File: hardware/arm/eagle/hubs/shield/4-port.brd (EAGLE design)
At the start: 31.5 x 58 mm, 11 parts

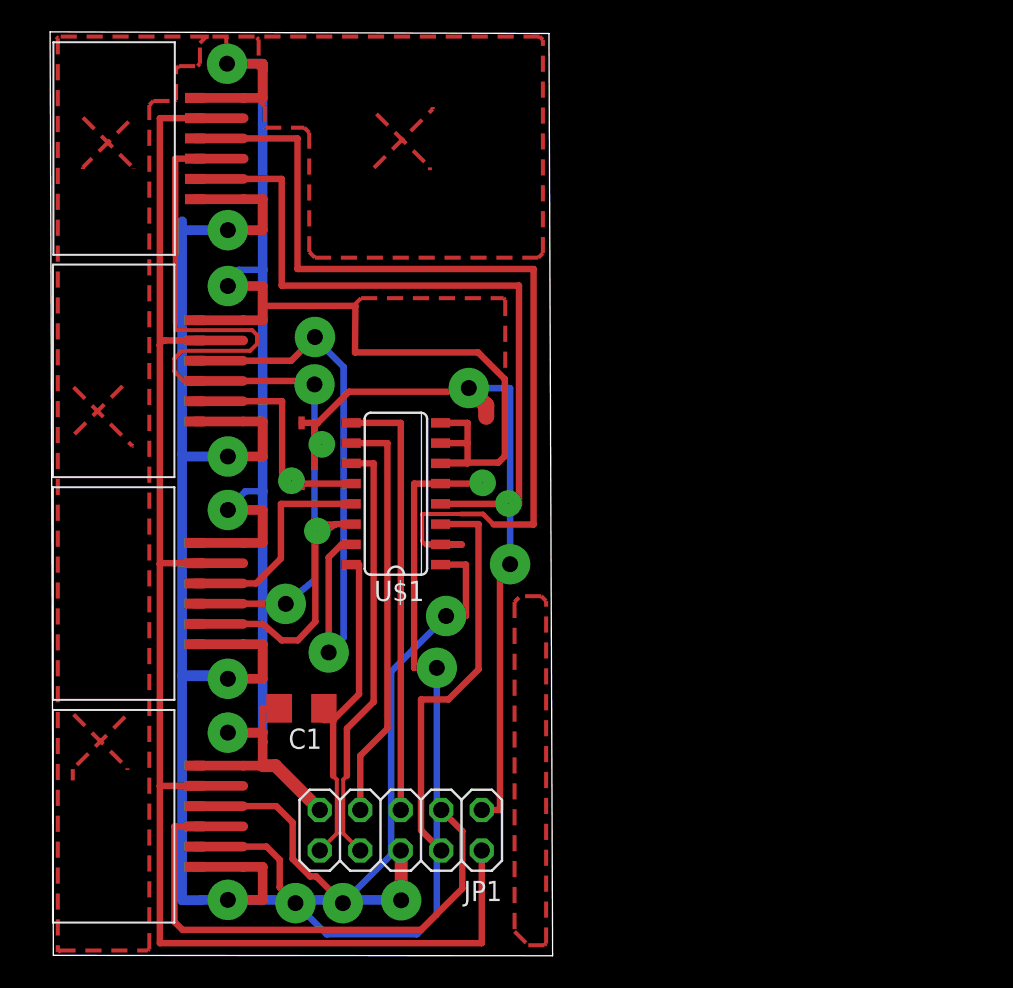
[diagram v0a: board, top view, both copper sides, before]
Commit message: 4 port shield pcb
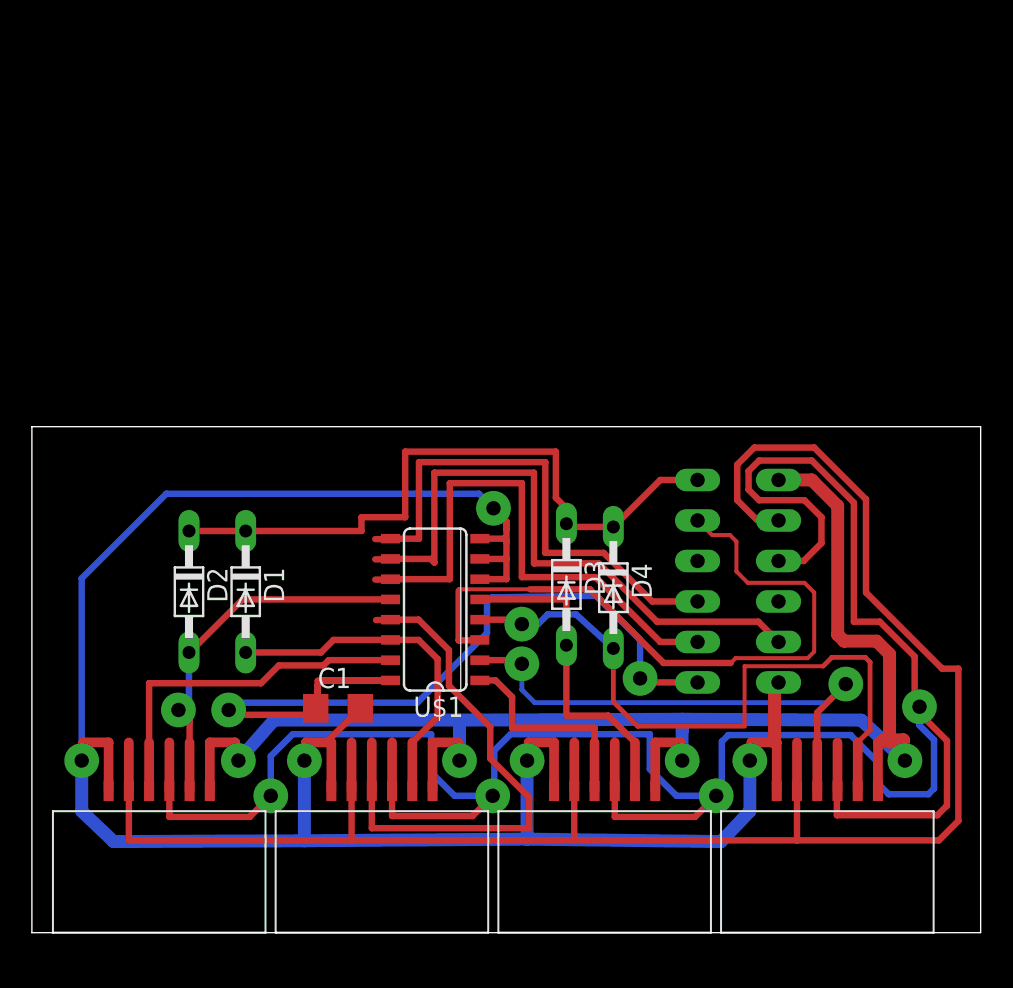
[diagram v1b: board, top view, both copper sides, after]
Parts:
- removed JP1: (no value), pinhead:2X05
- removed U$6, U$8, U$9: DIODE, gumyns:DIL_DIODE_SMD
- added D1, D2, D3, D4: BAS15, diode:DO34-7
- U$3: value DIODE -> HUB_PORT; device gumyns:DIL_DIODE_SMD -> gumyns:HUB_PORT
- moved U$7 63.7 mm to (48.3, 3.81), turned to 0 degrees
- moved U$4 31.9 mm to (6.35, 3.81), turned to 0 degrees
- moved U$5 30.7 mm to (34.3, 3.81), turned to 0 degrees
- moved U$3 27.9 mm to (43.0, 18.2), turned to 90 degrees
- moved U$2 24.3 mm to (20.3, 3.81), turned to 0 degrees
- moved U$1 7.67 mm to (24.0, 20.3)
- moved C1 2.29 mm to (17.9, 14.1), turned to 0 degrees
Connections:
- net 12V: now also U$3.12V; no longer JP1.6
- net 3.3V: now also U$3.3.3V; no longer JP1.10
- net A: now also U$3.A; no longer JP1.8
- net B: now also U$3.B; no longer JP1.7
- net C: now also U$3.C; no longer JP1.5
- net DATA: now also U$3.DATA; no longer JP1.3
- net GND: now also U$3.GND; no longer JP1.9
- net INT: now also D1.C, D2.C, D3.C, D4.C, U$3.INT; no longer JP1.1, U$3.1, U$6.1, U$8.1, U$9.1
- net INT0: now also D1.A; no longer U$3.2
- net INT1: now also D2.A; no longer U$9.2
- net INT2: now also D3.A; no longer U$6.2
- net INT3: now also D4.A; no longer U$8.2
- net NSS: now also U$3.NSS; no longer JP1.2
- net SCK: now also U$3.SCK; no longer JP1.4
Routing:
- net N$8: track 194.7 -> 0.00 mm
- net DATA: track 80.3 -> 143.9 mm, vias 2 -> 4
- net N$19: track 46.7 -> 0.00 mm
- net 3.3V: track 20.9 -> 56.0 mm, vias 0 -> 2
- net INT2: track 49.6 -> 17.7 mm, vias 2 -> 0
- net SCK2: track 36.9 -> 10.5 mm, vias 2 -> 0
- net SCK3: track 55.2 -> 30.0 mm, vias 0 -> 2
- net SCK0: track 10.9 -> 33.9 mm
- net NSS: track 86.7 -> 106.8 mm
- net SCK: track 25.9 -> 43.1 mm
- net N$7: track 14.6 -> 0.00 mm
- net SCK1: track 33.8 -> 19.5 mm, vias 2 -> 0
- net 12V: track 96.3 -> 83.4 mm, vias 5 -> 4
- net B: track 26.0 -> 38.8 mm
- net GND: track 117.9 -> 128.1 mm, vias 4 -> 5
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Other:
- board size 31.5 x 58 mm -> 59.5 x 31.7 mm
